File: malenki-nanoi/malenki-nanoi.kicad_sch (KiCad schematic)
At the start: 23 parts, among them J1 Conn_01x02_Male, J2 Conn_01x03, J3 Conn_01x02, J5 Conn_01x02_Male, J6 Conn_01x02_Male, J7 Conn_01x02_Male, U2 AIC1734-33GUTR, U3 ATtiny1617-M, U5 DRV8837DSGR, U6 DRV8837DSGR, U7 DRV8837DSGR

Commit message: Another crazy version of rx
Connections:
- net GND: now also U2.1 (GND)
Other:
- moved on the sheet: U2
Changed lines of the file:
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@@
-(kicad_sch (version 20200310) (host eeschema "5.99.0-unknown-5cf474e~101~ubuntu18.04.1")
-  (page "A4")
+(kicad_sch (version 20200512) (host eeschema "5.99.0-unknown-92ce7ca~101~ubuntu18.04.1")
+  (page 1 2)
+  (paper "A4")
   (title_block
     (title "Malenki-Nano i")
@@
     (company "Mark Robson")
   )
+  (junction (at 45.72 55.88))
+  (junction (at 57.15 48.26))
+  (junction (at 57.15 55.88))
+  (junction (at 63.5 48.26))
+  (junction (at 63.5 55.88))
+  (junction (at 80.01 55.88))
   (junction (at 91.44 119.38))
-  (junction (at 45.72 55.88))
-  (junction (at 57.15 55.88))
+  (junction (at 92.71 48.26))
+  (junction (at 106.68 156.21))
+  (junction (at 210.82 143.51))
+  (junction (at 212.09 93.98))
   (junction (at 214.63 43.18))
-  (junction (at 57.15 48.26))
-  (junction (at 63.5 55.88))
+  (junction (at 215.9 153.67))
   (junction (at 217.17 104.14))
-  (junction (at 212.09 93.98))
-  (junction (at 63.5 48.26))
-  (junction (at 210.82 143.51))
-  (junction (at 215.9 153.67))
-  (junction (at 106.68 156.21))
-  (junction (at 92.71 48.26))
   (junction (at 219.71 53.34))
   (no_connect (at 142.24 124.46))
+  (no_connect (at 142.24 119.38))
+  (no_connect (at 142.24 121.92))
   (no_connect (at 142.24 127))
-  (no_connect (at 142.24 121.92))
-  (no_connect (at 142.24 119.38))
   (wire (pts (xy 38.1 48.26) (xy 57.15 48.26)))
   (wire (pts (xy 38.1 50.8) (xy 45.72 50.8)))
@@
   (wire (pts (xy 57.15 48.26) (xy 63.5 48.26)))
   (wire (pts (xy 57.15 55.88) (xy 63.5 55.88)))
-  (wire (pts (xy 63.5 48.26) (xy 71.12 48.26)))
-  (wire (pts (xy 63.5 55.88) (xy 92.71 55.88)))
-  (wire (pts (xy 86.36 48.26) (xy 92.71 48.26)))
+  (wire (pts (xy 63.5 48.26) (xy 72.39 48.26)))
+  (wire (pts (xy 63.5 55.88) (xy 80.01 55.88)))
+  (wire (pts (xy 80.01 55.88) (xy 92.71 55.88)))
+  (wire (pts (xy 87.63 48.26) (xy 92.71 48.26)))
   (wire (pts (xy 91.44 116.84) (xy 91.44 119.38)))
   (wire (pts (xy 91.44 116.84) (xy 111.76 116.84)))
@@
     )
   )
-  (symbol (lib_id "mal_nano:HT7233") (at 78.74 44.45 0) (unit 1)
-    (property "Reference" "U2" (id 0) (at 78.74 42.1132 0))
-    (property "Value" "AIC1734-33GUTR" (id 1) (at 78.74 44.4246 0))
-    (property "Footprint" "Package_TO_SOT_SMD:SOT-23" (id 2) (at 78.74 44.45 0)
-      (effects (font (size 1.27 1.27)) hide)
-    )
-    (property "Datasheet" "" (id 3) (at 78.74 44.45 0)
-      (effects (font (size 1.27 1.27)) hide)
-    )
-    (property "Partnum" "C211659" (id 4) (at 78.74 44.45 0)
-      (effects (font (size 1.27 1.27)) hide)
-    )
-    (property "LCSC" "C211659" (id 5) (at 78.74 44.45 0)
+  (symbol (lib_id "mal_nano:HT7233") (at 80.01 44.45 0) (unit 1)
+    (property "Reference" "U2" (id 0) (at 80.01 42.1132 0))
+    (property "Value" "AIC1734-33GUTR" (id 1) (at 80.01 44.4246 0))
+    (property "Footprint" "Package_TO_SOT_SMD:SOT-23" (id 2) (at 80.01 44.45 0)
+      (effects (font (size 1.27 1.27)) hide)
+    )
+    (property "Datasheet" "" (id 3) (at 80.01 44.45 0)
+      (effects (font (size 1.27 1.27)) hide)
+    )
+    (property "Partnum" "C211659" (id 4) (at 80.01 44.45 0)
+      (effects (font (size 1.27 1.27)) hide)
+    )
+    (property "LCSC" "C211659" (id 5) (at 80.01 44.45 0)
       (effects (font (size 1.27 1.27)) hide)
     )
@@
     (stroke (width 0.1524) (color 132 0 132 1))
     (fill (color 255 255 255 0.0000))
-    (property "Reference" "radio" (id 4) (at 22.86 111.1245 0)
+    (property "Sheet name" "radio" (id 0) (at 22.86 111.1245 0)
       (effects (font (size 1.27 1.27)) (justify left bottom))
     )
-    (property "Value" "radio.kicad_sch" (id 5) (at 22.86 175.7685 0)
+    (property "Sheet file" "radio.kicad_sch" (id 1) (at 22.86 175.7685 0)
       (effects (font (size 1.27 1.27)) (justify left top))
     )

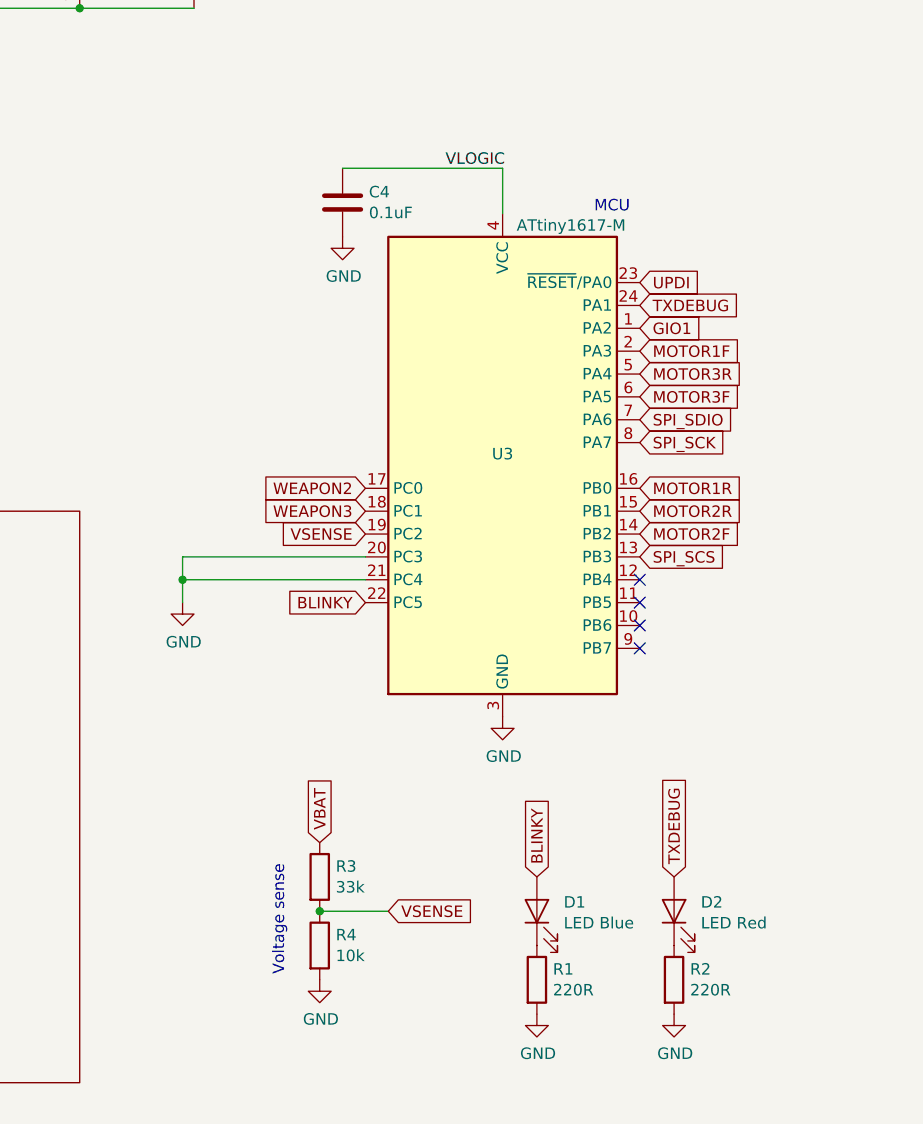
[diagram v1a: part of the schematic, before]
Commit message: A version of Malenki-nano with radio included on board
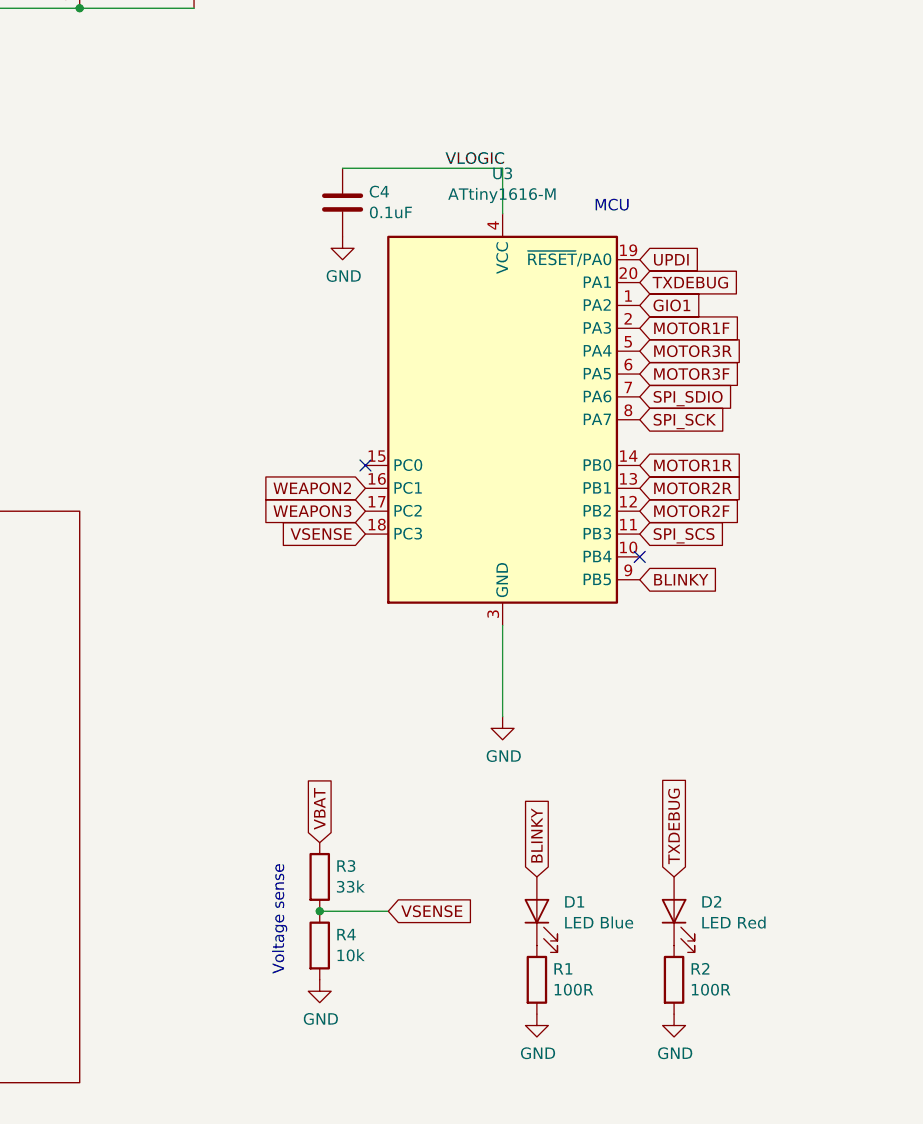
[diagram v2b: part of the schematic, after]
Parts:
- removed U3: ATtiny1617-M, malenki-nano:qfn24-hand1, symbol MCU_Microchip_ATtiny:ATtiny1617-M
- added U3: ATtiny1616-M, Package_DFN_QFN:VQFN-20-1EP_3x3mm_P0.4mm_EP1.7x1.7mm, symbol MCU_Microchip_ATtiny:ATtiny1616-M
- D1: footprint LED_SMD:LED_0805_2012Metric_Castellated -> LED_SMD:LED_0603_1608Metric_Castellated; LCSC C2293 -> C72041
- D2: footprint LED_SMD:LED_0805_2012Metric_Castellated -> LED_SMD:LED_0603_1608Metric_Castellated; LCSC C84256 -> C2286
- R1, R2: value 220R -> 100R; LCSC C22962 -> C22775; Partnum C22962 -> (none)
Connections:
- net BLINKY: now also U3.9 (PB5)
- net GIO1: now also U3.1 (PA2)
- net GND: now also U3.21 (GND), U3.3 (GND)
- net MOTOR1F: now also U3.2 (PA3)
- net MOTOR1R: now also U3.14 (PB0)
- net MOTOR2F: now also U3.12 (PB2)
- net MOTOR2R: now also U3.13 (PB1)
- net MOTOR3F: now also U3.6 (PA5)
- net MOTOR3R: now also U3.5 (PA4)
- net SPI_SCK: now also U3.8 (PA7)
- net SPI_SCS: now also U3.11 (PB3)
- net SPI_SDIO: now also U3.7 (PA6)
- net TXDEBUG: now also U3.20 (PA1)
- net UPDI: now also U3.19 (~RESET~/PA0)
- net VLOGIC: now also U3.4 (VCC)
- net VSENSE: now also U3.18 (PC3)
- net WEAPON2: now also U3.16 (PC1)
- net WEAPON3: now also U3.17 (PC2)
- no-connect marks 4 -> 2
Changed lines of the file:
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@@
-(kicad_sch (version 20200512) (host eeschema "5.99.0-unknown-92ce7ca~101~ubuntu18.04.1")
+(kicad_sch (version 20200512) (host eeschema "5.99.0-unknown-c8476d6~101~ubuntu18.04.1")
   (page 1 2)
   (paper "A4")
@@
   (junction (at 63.5 55.88))
   (junction (at 80.01 55.88))
-  (junction (at 91.44 119.38))
   (junction (at 92.71 48.26))
   (junction (at 106.68 156.21))
@@
   (junction (at 217.17 104.14))
   (junction (at 219.71 53.34))
-  (no_connect (at 142.24 124.46))
-  (no_connect (at 142.24 119.38))
-  (no_connect (at 142.24 121.92))
-  (no_connect (at 142.24 127))
+  (no_connect (at 111.76 106.68))
+  (no_connect (at 142.24 116.84))
   (wire (pts (xy 38.1 48.26) (xy 57.15 48.26)))
   (wire (pts (xy 38.1 50.8) (xy 45.72 50.8)))
@@
   (wire (pts (xy 80.01 55.88) (xy 92.71 55.88)))
   (wire (pts (xy 87.63 48.26) (xy 92.71 48.26)))
-  (wire (pts (xy 91.44 116.84) (xy 91.44 119.38)))
-  (wire (pts (xy 91.44 116.84) (xy 111.76 116.84)))
-  (wire (pts (xy 91.44 119.38) (xy 91.44 121.92)))
   (wire (pts (xy 92.71 48.26) (xy 104.14 48.26)))
-  (wire (pts (xy 111.76 119.38) (xy 91.44 119.38)))
   (wire (pts (xy 114.3 156.21) (xy 106.68 156.21)))
   (wire (pts (xy 127 73.66) (xy 109.22 73.66)))
   (wire (pts (xy 127 73.66) (xy 127 78.74)))
+  (wire (pts (xy 127 124.46) (xy 127 134.62)))
   (wire (pts (xy 129.54 45.72) (xy 143.51 45.72)))
   (wire (pts (xy 165.1 49.53) (xy 168.91 49.53)))
@@
     (effects (font (size 1.27 1.27)) (justify right))
   )
-  (global_label "BLINKY" (shape input) (at 111.76 121.92 180)
-    (effects (font (size 1.27 1.27)) (justify right))
-  )
   (global_label "VSENSE" (shape input) (at 114.3 156.21 0)
     (effects (font (size 1.27 1.27)) (justify left))
@@
     (effects (font (size 1.27 1.27)) (justify left))
   )
-  (global_label "UPDI" (shape input) (at 142.24 86.36 0)
-    (effects (font (size 1.27 1.27)) (justify left))
-  )
-  (global_label "TXDEBUG" (shape input) (at 142.24 88.9 0)
-    (effects (font (size 1.27 1.27)) (justify left))
-  )
-  (global_label "GIO1" (shape input) (at 142.24 91.44 0)
-    (effects (font (size 1.27 1.27)) (justify left))
-  )
-  (global_label "MOTOR1F" (shape input) (at 142.24 93.98 0)
-    (effects (font (size 1.27 1.27)) (justify left))
-  )
-  (global_label "MOTOR3R" (shape input) (at 142.24 96.52 0)
-    (effects (font (size 1.27 1.27)) (justify left))
-  )
-  (global_label "MOTOR3F" (shape input) (at 142.24 99.06 0)
-    (effects (font (size 1.27 1.27)) (justify left))
-  )
-  (global_label "SPI_SDIO" (shape input) (at 142.24 101.6 0)
-    (effects (font (size 1.27 1.27)) (justify left))
-  )
-  (global_label "SPI_SCK" (shape input) (at 142.24 104.14 0)
-    (effects (font (size 1.27 1.27)) (justify left))
-  )
-  (global_label "MOTOR1R" (shape input) (at 142.24 109.22 0)
-    (effects (font (size 1.27 1.27)) (justify left))
-  )
-  (global_label "MOTOR2R" (shape input) (at 142.24 111.76 0)
-    (effects (font (size 1.27 1.27)) (justify left))
-  )
-  (global_label "MOTOR2F" (shape input) (at 142.24 114.3 0)
-    (effects (font (size 1.27 1.27)) (justify left))
-  )
-  (global_label "SPI_SCS" (shape input) (at 142.24 116.84 0)
+  (global_label "UPDI" (shape input) (at 142.24 83.82 0)
+    (effects (font (size 1.27 1.27)) (justify left))
+  )
+  (global_label "TXDEBUG" (shape input) (at 142.24 86.36 0)
+    (effects (font (size 1.27 1.27)) (justify left))
+  )
+  (global_label "GIO1" (shape input) (at 142.24 88.9 0)
+    (effects (font (size 1.27 1.27)) (justify left))
+  )
+  (global_label "MOTOR1F" (shape input) (at 142.24 91.44 0)
+    (effects (font (size 1.27 1.27)) (justify left))
+  )
+  (global_label "MOTOR3R" (shape input) (at 142.24 93.98 0)
+    (effects (font (size 1.27 1.27)) (justify left))
+  )
+  (global_label "MOTOR3F" (shape input) (at 142.24 96.52 0)
+    (effects (font (size 1.27 1.27)) (justify left))
+  )
+  (global_label "SPI_SDIO" (shape input) (at 142.24 99.06 0)
+    (effects (font (size 1.27 1.27)) (justify left))
+  )
+  (global_label "SPI_SCK" (shape input) (at 142.24 101.6 0)
+    (effects (font (size 1.27 1.27)) (justify left))
+  )
+  (global_label "MOTOR1R" (shape input) (at 142.24 106.68 0)
+    (effects (font (size 1.27 1.27)) (justify left))
+  )
+  (global_label "MOTOR2R" (shape input) (at 142.24 109.22 0)
+    (effects (font (size 1.27 1.27)) (justify left))
+  )
+  (global_label "MOTOR2F" (shape input) (at 142.24 111.76 0)
+    (effects (font (size 1.27 1.27)) (justify left))
+  )
+  (global_label "SPI_SCS" (shape input) (at 142.24 114.3 0)
+    (effects (font (size 1.27 1.27)) (justify left))
+  )
+  (global_label "BLINKY" (shape input) (at 142.24 119.38 0)
     (effects (font (size 1.27 1.27)) (justify left))
   )
@@
     )
   )
-  (symbol (lib_id "malenki-nano-rescue:GND-power") (at 91.44 121.92 0) (unit 1)
-    (property "Reference" "#PWR0101" (id 0) (at 91.44 128.27 0)
-      (effects (font (size 1.27 1.27)) hide)
-    )
-    (property "Value" "GND" (id 1) (at 91.567 126.3142 0))
-    (property "Footprint" "" (id 2) (at 91.44 121.92 0)
-      (effects (font (size 1.27 1.27)) hide)
-    )
-    (property "Datasheet" "" (id 3) (at 91.44 121.92 0)
-      (effects (font (size 1.27 1.27)) hide)
-    )
-  )
   (symbol (lib_id "malenki-nano-rescue:GND-power") (at 106.68 163.83 0) (unit 1)
     (property "Reference" "#PWR07" (id 0) (at 106.68 170.18 0)
@@
       (effects (font (size 1.27 1.27)) (justify left))
     )
-    (property "Value" "220R" (id 1) (at 132.588 164.973 0)
+    (property "Value" "100R" (id 1) (at 132.588 164.973 0)
       (effects (font (size 1.27 1.27)) (justify left))
     )
@@
       (effects (font (size 1.27 1.27)) hide)
     )
-    (property "Partnum" "C22962" (id 4) (at 130.81 163.83 0)
-      (effects (font (size 1.27 1.27)) hide)
-    )
-    (property "LCSC" "C22962" (id 5) (at 130.81 163.83 0)
+    (property "Partnum" "" (id 4) (at 130.81 163.83 0)
+      (effects (font (size 1.27 1.27)) hide)
+    )
+    (property "LCSC" "C22775" (id 5) (at 130.81 163.83 0)
       (effects (font (size 1.27 1.27)) hide)
     )
@@
       (effects (font (size 1.27 1.27)) (justify left))
     )
-    (property "Value" "220R" (id 1) (at 147.828 164.973 0)
+    (property "Value" "100R" (id 1) (at 147.828 164.973 0)
       (effects (font (size 1.27 1.27)) (justify left))
     )
@@
       (effects (font (size 1.27 1.27)) hide)
     )
-    (property "Partnum" "C22962" (id 4) (at 146.05 163.83 0)
-      (effects (font (size 1.27 1.27)) hide)
-    )
-    (property "LCSC" "C22962" (id 5) (at 146.05 163.83 0)
+    (property "Partnum" "" (id 4) (at 146.05 163.83 0)
+      (effects (font (size 1.27 1.27)) hide)
+    )
+    (property "LCSC" "C22775" (id 5) (at 146.05 163.83 0)
       (effects (font (size 1.27 1.27)) hide)
     )
@@
       (effects (font (size 1.27 1.27)) (justify right))
     )
-    (property "Footprint" "LED_SMD:LED_0805_2012Metric_Castellated" (id 2) (at 130.81 156.21 0)
+    (property "Footprint" "LED_SMD:LED_0603_1608Metric_Castellated" (id 2) (at 130.81 156.21 0)
       (effects (font (size 1.27 1.27)) hide)
     )
@@
       (effects (font (size 1.27 1.27)) hide)
     )
-    (property "LCSC" "C2293" (id 4) (at 130.81 156.21 0)
+    (property "LCSC" "C72041" (id 4) (at 130.81 156.21 0)
       (effects (font (size 1.27 1.27)) hide)
     )
@@
       (effects (font (size 1.27 1.27)) (justify right))
     )
-    (property "Footprint" "LED_SMD:LED_0805_2012Metric_Castellated" (id 2) (at 146.05 156.21 0)
+    (property "Footprint" "LED_SMD:LED_0603_1608Metric_Castellated" (id 2) (at 146.05 156.21 0)
       (effects (font (size 1.27 1.27)) hide)
     )
@@
       (effects (font (size 1.27 1.27)) hide)
     )
-    (property "LCSC" "C84256" (id 4) (at 146.05 156.21 0)
+    (property "LCSC" "C2286" (id 4) (at 146.05 156.21 0)
       (effects (font (size 1.27 1.27)) hide)
     )
@@
     )
   )
-  (symbol (lib_id "MCU_Microchip_ATtiny:ATtiny1617-M") (at 127 106.68 0) (unit 1)
-    (property "Reference" "U3" (id 0) (at 127 105.41 0))
-    (property "Value" "ATtiny1617-M" (id 1) (at 134.62 80.01 0))
-    (property "Footprint" "malenki-nano:qfn24-hand1" (id 2) (at 127 106.68 0)
+  (symbol (lib_id "MCU_Microchip_ATtiny:ATtiny1616-M") (at 127 101.6 0) (unit 1)
+    (property "Reference" "U3" (id 0) (at 127 74.2758 0))
+    (property "Value" "ATtiny1616-M" (id 1) (at 127 76.5745 0))
+    (property "Footprint" "Package_DFN_QFN:VQFN-20-1EP_3x3mm_P0.4mm_EP1.7x1.7mm" (id 2) (at 127 101.6 0)
       (effects (font (size 1.27 1.27) italic) hide)
     )
-    (property "Datasheet" "" (id 3) (at 127 106.68 0)
-      (effects (font (size 1.27 1.27)) hide)
-    )
-    (property "Partnum" "C194193" (id 4) (at 127 106.68 0)
-      (effects (font (size 1.27 1.27)) hide)
-    )
-    (property "LCSC" "C194193" (id 5) (at 127 106.68 0)
+    (property "Datasheet" "http://ww1.microchip.com/downloads/en/DeviceDoc/ATtiny3216_ATtiny1616-data-sheet-40001997B.pdf" (id 3) (at 127 101.6 0)
       (effects (font (size 1.27 1.27)) hide)
     )
@@
     (path "/4ab669ca-0b13-42d2-a107-ab12d0523cd2" (reference "#PWR08") (unit 1))
     (path "/2104630b-94b6-4ebd-9ced-a396e4ce9986" (reference "#PWR011") (unit 1))
-    (path "/979b4a07-f759-4309-99c2-b59f64b14013" (reference "#PWR0101") (unit 1))
     (path "/ef4e08bd-4800-4b22-a140-a695bc8fa530" (reference "#PWR0102") (unit 1))
     (path "/fb14aff6-0ae4-4113-b9ef-4ef1bcc9ac29" (reference "#PWR0103") (unit 1))
@@
     (path "/c993b812-4481-4a51-89b1-627aff73a2eb" (reference "R4") (unit 1))
     (path "/3494058c-6394-401b-a0c4-3fc485b2e763" (reference "U2") (unit 1))
-    (path "/9ca9b127-3e2d-49fa-9639-343756033fc3" (reference "U3") (unit 1))
+    (path "/d3e2ff1e-c2a5-4ec5-82d1-74bc0058ad00" (reference "U3") (unit 1))
     (path "/4f9b39f2-430c-4379-8abe-54544cc740e1" (reference "U5") (unit 1))
     (path "/bed320e4-aa81-4a00-a923-0e13227175f8" (reference "U6") (unit 1))
